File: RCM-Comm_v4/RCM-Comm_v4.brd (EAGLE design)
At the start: 50.8 x 66 mm, 28 parts, among them J1 BLACKFIN_HEADER, J2 2199230-4

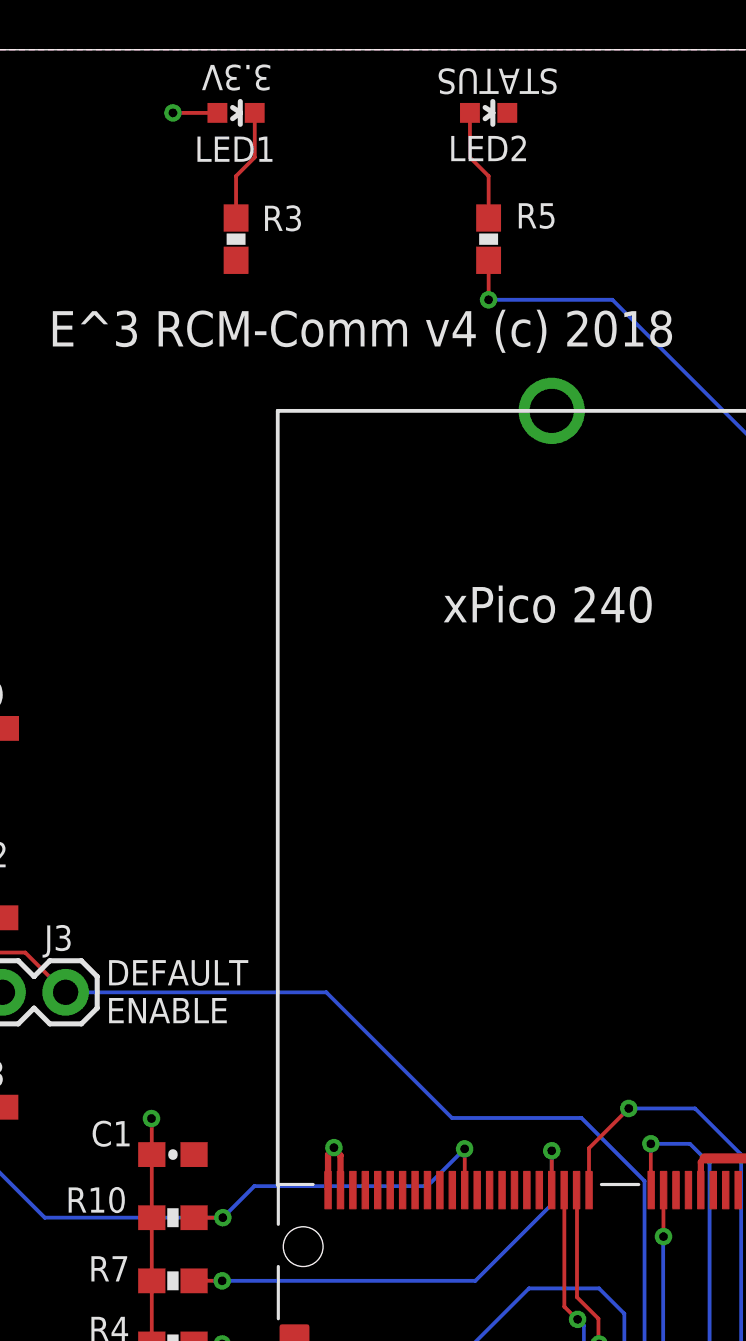
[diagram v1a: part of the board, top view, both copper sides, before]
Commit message: Added WLAN Led on configurable pin (CP) #1.
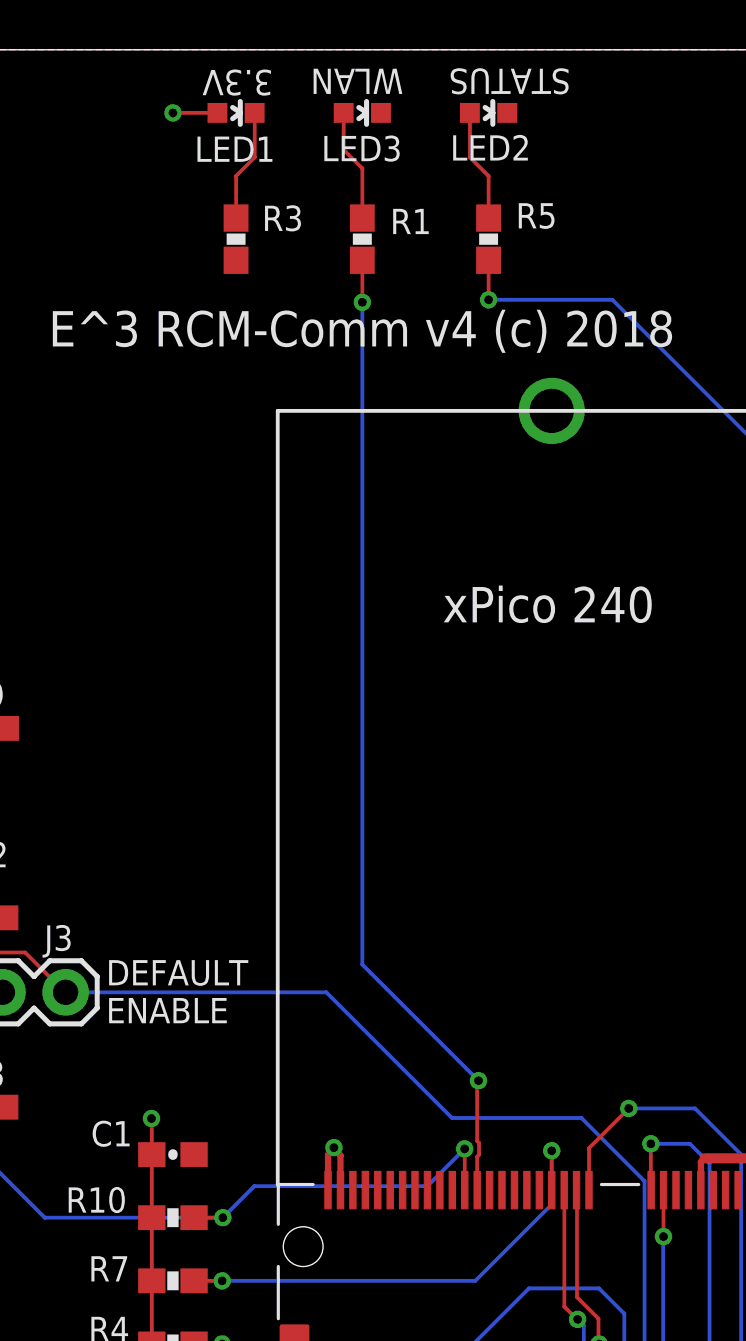
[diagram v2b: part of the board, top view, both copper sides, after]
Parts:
- added LED3: GREEN, spark_fun:LED-0603
- added R1: 330, spark_fun:0603-RES
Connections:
- removed net N$68: J2.50
- new net N$2: LED3.A, R1.2
- new net WLAN0: J2.50, R1.1
- net GND: now also LED3.C
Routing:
- net WLAN0: track 0.00 -> 39.5 mm, vias 0 -> 2
- net N$2: track 0.00 -> 4.54 mm
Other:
- board text added: "WLAN"
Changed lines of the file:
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@@
 <circle x="47.498" y="5.08" radius="0.254" width="0.254" layer="21"/>
 <text x="15.3162" y="54.102" size="1.4224" layer="21" font="vector">E^3 RCM-Comm v4 (c) 2018</text>
-<text x="35.8394" y="65.278" size="1.016" layer="21" font="vector" ratio="10" rot="SR180">STATUS</text>
-<text x="24.3332" y="65.4304" size="1.016" layer="21" font="vector" ratio="10" rot="SR180">3.3V</text>
+<text x="36.322" y="65.278" size="1.016" layer="21" font="vector" ratio="10" rot="SR180">STATUS</text>
+<text x="24.3586" y="65.2272" size="1.016" layer="21" font="vector" ratio="10" rot="SR180">3.3V</text>
 <text x="3.302" y="39.8526" size="1.016" layer="21" font="vector" ratio="10" rot="SR0">WAKE</text>
 <text x="3.302" y="32.2326" size="1.016" layer="21" font="vector" ratio="10" rot="SR0">DEAFAULT</text>
@@
 <text x="17.6276" y="26.8732" size="1.016" layer="21" font="vector" ratio="10" rot="SR0">DEFAULT
 ENABLE</text>
+<text x="29.591" y="65.278" size="1.016" layer="21" font="vector" ratio="10" rot="SR180">WLAN</text>
 </plain>
 <attributes>
@@
 </element>
 <element name="LED2" library="spark_fun" package="LED-0603" value="GREEN" x="33.02" y="63.5" smashed="yes" rot="R270">
-<attribute name="NAME" x="31.3944" y="61.5569" size="1.016" layer="25" font="vector" ratio="12"/>
-<attribute name="VALUE" x="30.8864" y="60.1345" size="1.016" layer="27" font="vector" ratio="12"/>
+<attribute name="NAME" x="31.4706" y="61.5823" size="1.016" layer="25" font="vector" ratio="12"/>
+<attribute name="VALUE" x="31.1912" y="60.2361" size="1.016" layer="27" font="vector" ratio="12"/>
 </element>
 <element name="R3" library="spark_fun" package="0603-RES" value="330" x="22.86" y="58.42" smashed="yes" rot="R90">
@@
 <attribute name="NAME" x="15.1384" y="29.7942" size="1.016" layer="25" font="vector" ratio="12"/>
 <attribute name="VALUE" x="12.192" y="26.0858" size="0.6096" layer="27" font="vector" ratio="20"/>
+</element>
+<element name="R1" library="spark_fun" package="0603-RES" value="330" x="27.94" y="58.42" smashed="yes" rot="R90">
+<attribute name="NAME" x="29.0576" y="58.6232" size="1.016" layer="25" font="vector" ratio="10"/>
+<attribute name="VALUE" x="29.0322" y="57.2008" size="1.016" layer="27" font="vector" ratio="10"/>
+</element>
+<element name="LED3" library="spark_fun" package="LED-0603" value="GREEN" x="27.94" y="63.5" smashed="yes" rot="R270">
+<attribute name="NAME" x="26.289" y="61.5569" size="1.016" layer="25" font="vector" ratio="10"/>
+<attribute name="VALUE" x="25.908" y="60.2361" size="1.016" layer="27" font="vector" ratio="10"/>
 </element>
 </elements>
@@
 <contactref element="S2" pad="1"/>
 <via x="35.56" y="51.5112" extent="1-16" drill="1.778"/>
+<contactref element="LED3" pad="C"/>
 </signal>
 <signal name="VCC">
@@
 <contactref element="J2" pad="54"/>
 </signal>
-<signal name="N$68">
-<contactref element="J2" pad="50"/>
-</signal>
 <signal name="N$69">
 <contactref element="J2" pad="48"/>
@@
 <wire x1="9.6266" y1="30.1752" x2="10.6934" y2="30.1752" width="0.1524" layer="1"/>
 </signal>
+<signal name="N$2">
+<contactref element="R1" pad="2"/>
+<contactref element="LED3" pad="A"/>
+<wire x1="27.94" y1="59.27" x2="27.94" y2="61.2648" width="0.1524" layer="1"/>
+<wire x1="27.19" y1="62.0148" x2="27.19" y2="63.5" width="0.1524" layer="1"/>
+<wire x1="27.94" y1="61.2648" x2="27.19" y2="62.0148" width="0.1524" layer="1"/>
+</signal>
+<signal name="WLAN0">
+<contactref element="R1" pad="1"/>
+<contactref element="J2" pad="50"/>
+<wire x1="32.56" y1="24.5082" x2="32.6136" y2="24.5618" width="0.1524" layer="1"/>
+<via x="32.6136" y="24.5618" extent="1-16" drill="0.35"/>
+<wire x1="32.56" y1="20.16" x2="32.56" y2="21.501575" width="0.1524" layer="1"/>
+<wire x1="32.56" y1="21.501575" x2="32.6362" y2="21.577775" width="0.1524" layer="1"/>
+<wire x1="32.6362" y1="21.577775" x2="32.6362" y2="22.059425" width="0.1524" layer="1"/>
+<wire x1="32.6362" y1="22.059425" x2="32.56" y2="22.135625" width="0.1524" layer="1"/>
+<wire x1="32.56" y1="22.135625" x2="32.56" y2="24.5082" width="0.1524" layer="1"/>
+<wire x1="32.6136" y1="24.5618" x2="27.94" y2="29.2354" width="0.1524" layer="16"/>
+<wire x1="27.94" y1="29.2354" x2="27.94" y2="55.88" width="0.1524" layer="16"/>
+<wire x1="27.94" y1="55.9054" x2="27.94" y2="55.88" width="0.1524" layer="16"/>
+<via x="27.94" y="55.88" extent="1-16" drill="0.35"/>
+<wire x1="27.94" y1="55.88" x2="27.94" y2="57.57" width="0.1524" layer="1"/>
+</signal>
 </signals>
